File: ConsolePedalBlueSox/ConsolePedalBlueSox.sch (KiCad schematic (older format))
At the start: 39 parts, among them J1 Conn_02x25_Counter_Clockwise, Q1 2N3904, Q2 2N3904, U1 RC4558

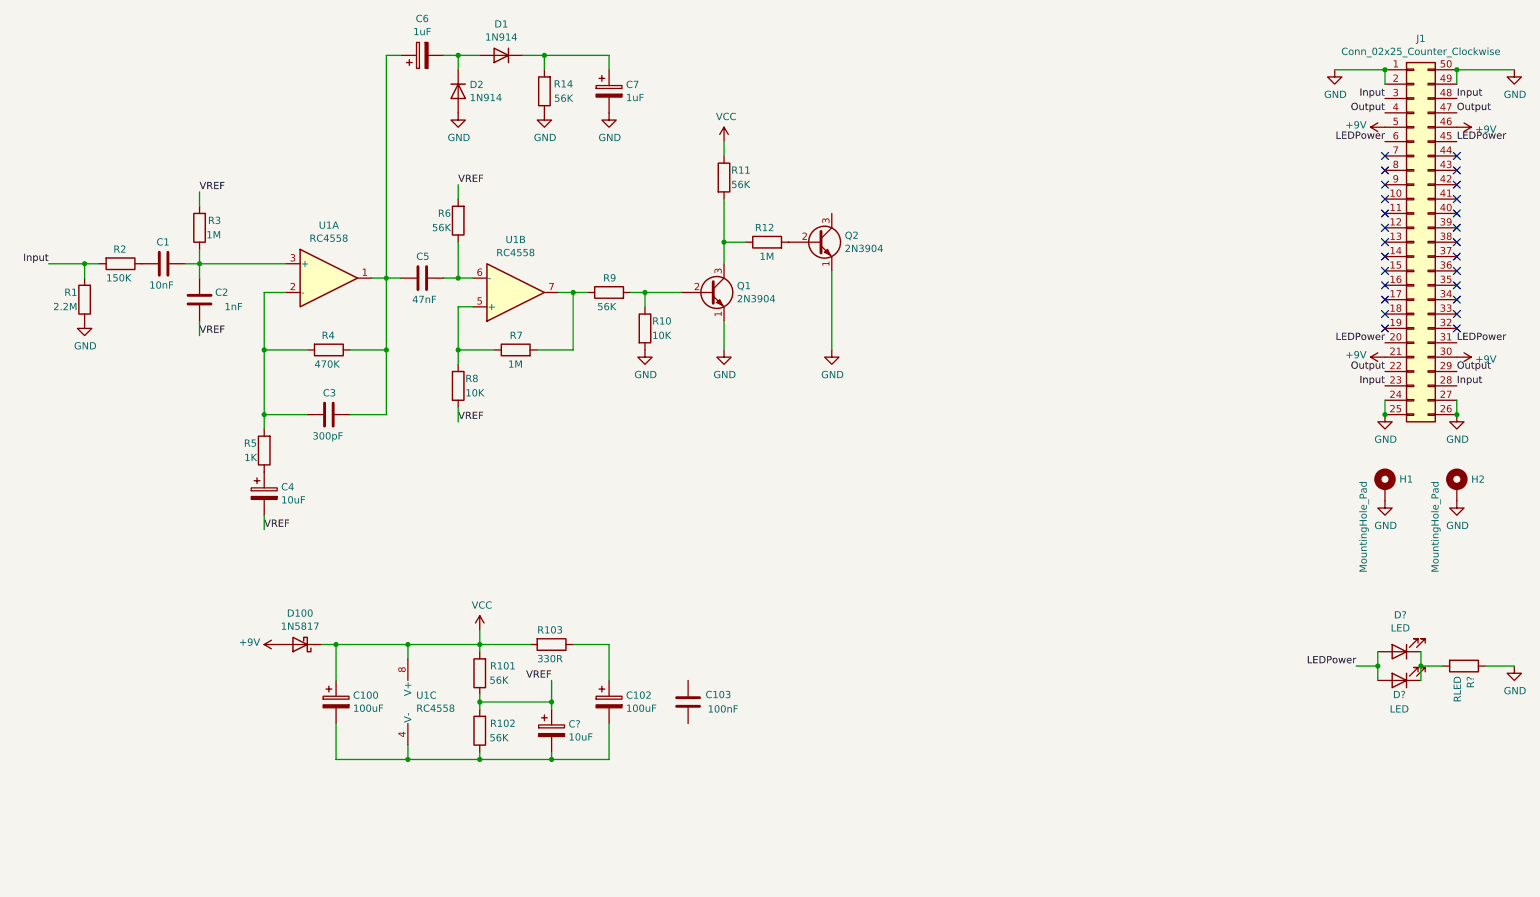
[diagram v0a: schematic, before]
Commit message: Finished schematic. Need to assign last footprints
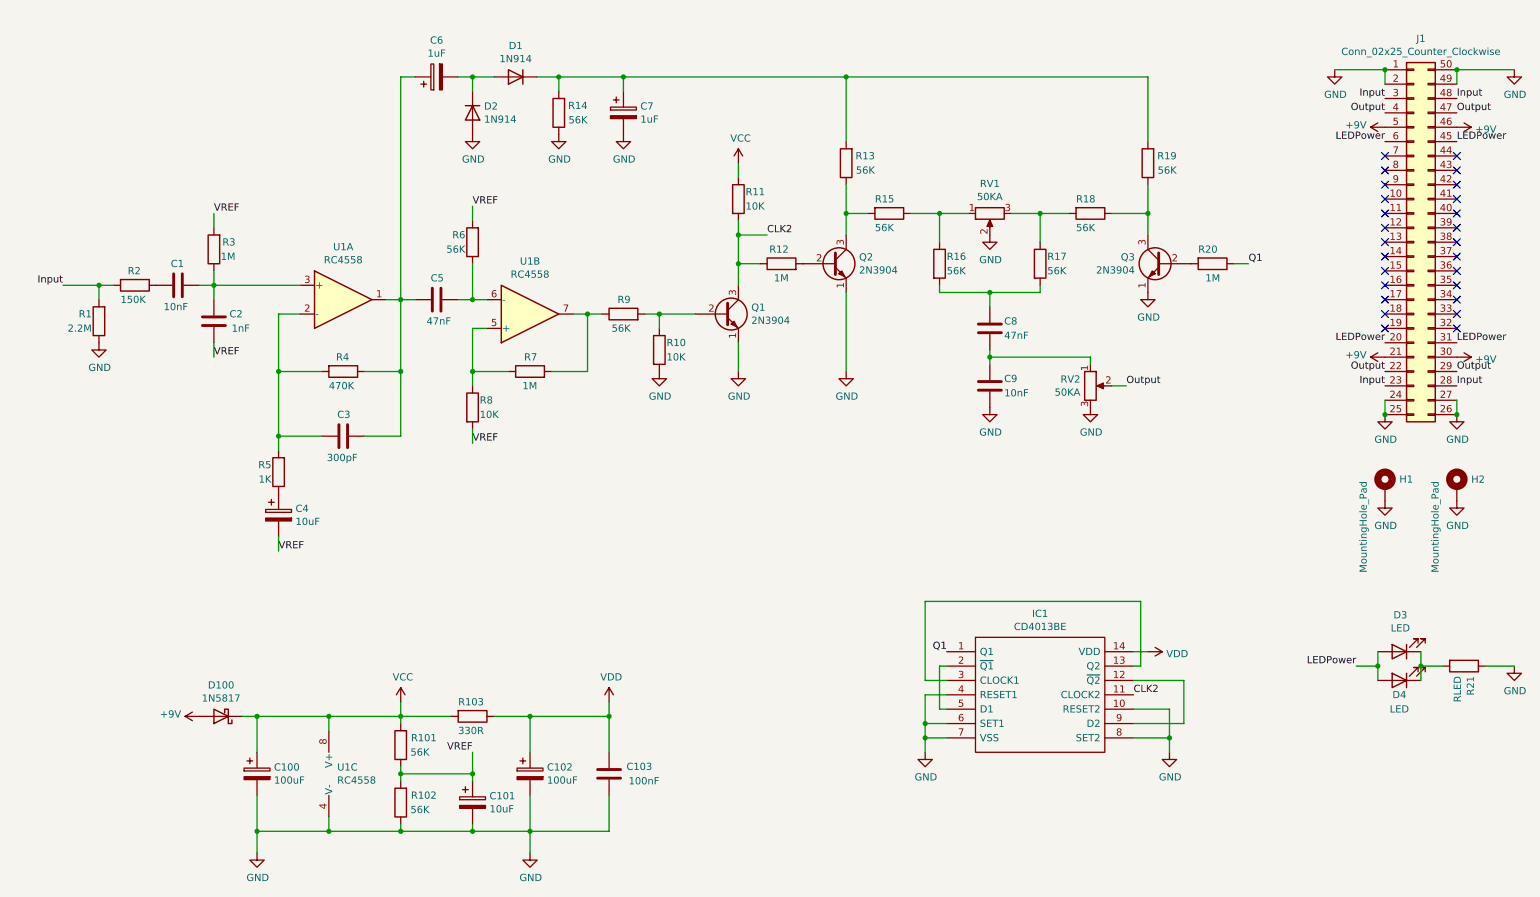
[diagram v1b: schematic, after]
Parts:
- added C8: 47nF, libraries:C_Flat_L7.2_H6.5, symbol Device:C
- added C9: 10nF, libraries:C_Flat_L7.2_H6.5, symbol Device:C
- added IC1: CD4013BE, Package_DIP:DIP-14_W7.62mm, symbol CD4013BE:CD4013BE
- added Q3: 2N3904, Package_TO_SOT_THT:TO-92_Inline, symbol Transistor_BJT:2N3904
- added R13, R15, R16, R17, R18, R19: 56K, Resistor_THT:R_Axial_DIN0207_L6.3mm_D2.5mm_P10.16mm_Horizontal, symbol Device:R
- added R20: 1M, Resistor_THT:R_Axial_DIN0207_L6.3mm_D2.5mm_P10.16mm_Horizontal, symbol Device:R
- added RV1, RV2: 50KA, Potentiometer_THT:Potentiometer_Bourns_PTV09A-1_Single_Vertical, symbol Device:R_POT
- R11: value 56K -> 10K
- U1: footprint (none) -> Package_DIP:DIP-8_W7.62mm
- gave numbers to parts that had none: 4
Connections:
- net GND: now also C100.2, C101.2, C102.2, C103.1, R102.1, U1.4 (V-), C9.2, IC1.10 (RESET2), IC1.4 (RESET1), IC1.6 (SET1), IC1.7 (VSS), IC1.8 (SET2), Q3.1 (E), RV1.2, RV2.3
- net Output: now also RV2.2
- net CLK2: now reaches Q1.3 (C), R11.2, R12.1
- net CLK2: now also IC1.11 (CLOCK2)
- net at Q2.3 (C): now also R13.1, R15.2
- net at C7.1, D1.1 (K), R14.2: now also R13.2, R19.2
- net VDD: now reaches C102.1, R103.1
- net VDD: now also C103.2, IC1.14 (VDD)
- new net: IC1.12 (~Q2), IC1.9 (D2)
- new net: IC1.13 (Q2), IC1.3 (CLOCK1)
- new net: IC1.2 (~Q1), IC1.5 (D1)
- new net: R15.1, R16.1, RV1.1
- new net: C8.1, R16.2, R17.2
- new net: R17.1, R18.2, RV1.3
- new net: C8.2, C9.1, RV2.1
- new net: Q3.3 (C), R18.1, R19.1
- new net: Q3.2 (B), R20.2
- new net Q1: IC1.1 (Q1), R20.1
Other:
- moved on the sheet: C1, C100, C101, C102, C103, C2, C3, C4, C5, C6, C7, D1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

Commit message: Placing components
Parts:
- C100, C102: footprint (none) -> libraries:CP_Radial_D6.3mm_P2.50mm_L11.0mm
- C101, C4: footprint (none) -> libraries:CP_Radial_D6.3mm_P2.50mm
- C6, C7: footprint (none) -> libraries:CP_Radial_D5.0mm_P2.00mm_L11.0mm
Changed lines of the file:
@@
 F 0 "C4" H 2468 4096 50  0000 L CNN
 F 1 "10uF" H 2468 4005 50  0000 L CNN
-F 2 "" H 2388 3900 50  0001 C CNN
+F 2 "libraries:CP_Radial_D6.3mm_P2.50mm" H 2388 3900 50  0001 C CNN
 F 3 "~" H 2350 4050 50  0001 C CNN
 	1    2350 4050
@@
 F 0 "C6" V 3705 1000 50  0000 C CNN
 F 1 "1uF" V 3614 1000 50  0000 C CNN
-F 2 "" H 3488 850 50  0001 C CNN
+F 2 "libraries:CP_Radial_D5.0mm_P2.00mm_L11.0mm" H 3488 850 50  0001 C CNN
 F 3 "~" H 3450 1000 50  0001 C CNN
 	1    3450 1000
@@
 F 0 "C7" H 4868 1296 50  0000 L CNN
 F 1 "1uF" H 4868 1205 50  0000 L CNN
-F 2 "" H 4788 1100 50  0001 C CNN
+F 2 "libraries:CP_Radial_D5.0mm_P2.00mm_L11.0mm" H 4788 1100 50  0001 C CNN
 F 3 "~" H 4750 1250 50  0001 C CNN
 	1    4750 1250
@@
 F 0 "C100" H 2318 5896 50  0000 L CNN
 F 1 "100uF" H 2318 5805 50  0000 L CNN
-F 2 "" H 2238 5700 50  0001 C CNN
+F 2 "libraries:CP_Radial_D6.3mm_P2.50mm_L11.0mm" H 2238 5700 50  0001 C CNN
 F 3 "~" H 2200 5850 50  0001 C CNN
 	1    2200 5850
@@
 F 0 "C101" H 3818 6096 50  0000 L CNN
 F 1 "10uF" H 3818 6005 50  0000 L CNN
-F 2 "" H 3738 5900 50  0001 C CNN
+F 2 "libraries:CP_Radial_D6.3mm_P2.50mm" H 3738 5900 50  0001 C CNN
 F 3 "~" H 3700 6050 50  0001 C CNN
 	1    3700 6050
@@
 F 0 "C102" H 4218 5896 50  0000 L CNN
 F 1 "100uF" H 4218 5805 50  0000 L CNN
-F 2 "" H 4138 5700 50  0001 C CNN
+F 2 "libraries:CP_Radial_D6.3mm_P2.50mm_L11.0mm" H 4138 5700 50  0001 C CNN
 F 3 "~" H 4100 5850 50  0001 C CNN
 	1    4100 5850
